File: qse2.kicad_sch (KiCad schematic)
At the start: 81 parts, among them J1 5-1814832-1, J2 5-1814832-1, J3 Conn_02x08_Odd_Even, J4 SJ-3524-SMT, J6 Conn_01x02, J7 B4B-XH-A_LF__SN_, U1 SN74LVC1G14DBV, U10 SN74LVC1G14DBV, U11 NCP114ASN330T1G, U2 SN74LVC1G14DBV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

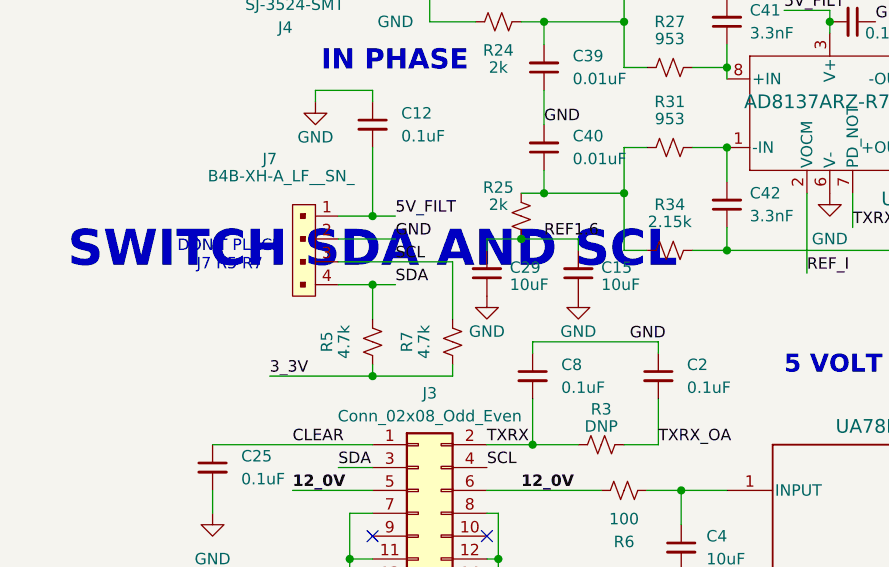
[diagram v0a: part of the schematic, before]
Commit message: Swapped SDA and SCL to correct pins.
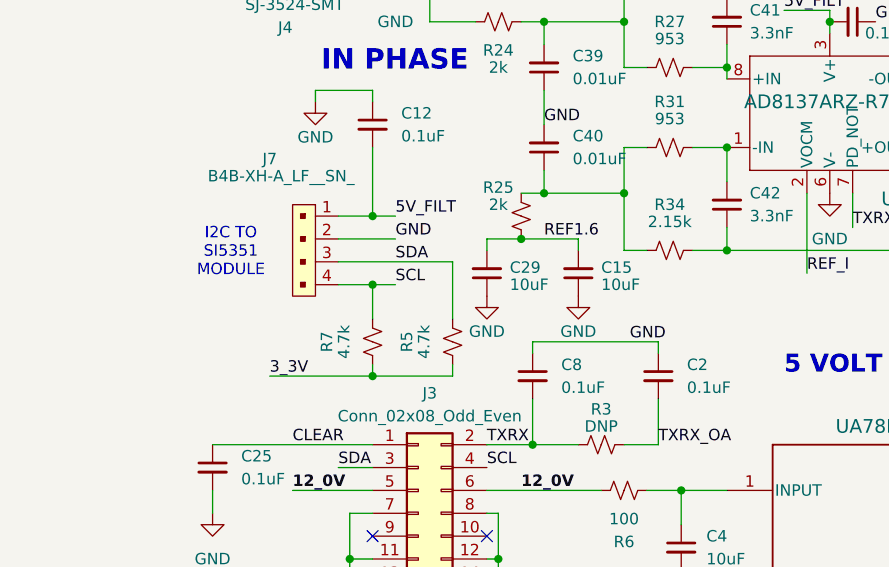
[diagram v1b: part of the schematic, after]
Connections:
- net SCL: now also J7.4; no longer J7.3
- net SDA: now also J7.3; no longer J7.4
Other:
- note added: "I2C TO SI5351 MODULE"
- note removed: "DON'T PLACE J7 R5 R7"
- note removed: "SWITCH SDA AND SCL"
- moved on the sheet: R5, R7
